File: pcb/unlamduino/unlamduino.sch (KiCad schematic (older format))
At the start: 34 parts, among them IC2 ATMEGA328-P, P3 CONN_01X08, P4 CONN_01X10, P5 CONN_01X06, P6 CONN_01X08, SW1 SW_PUSH, U1 LM2576, Y2 16MHz

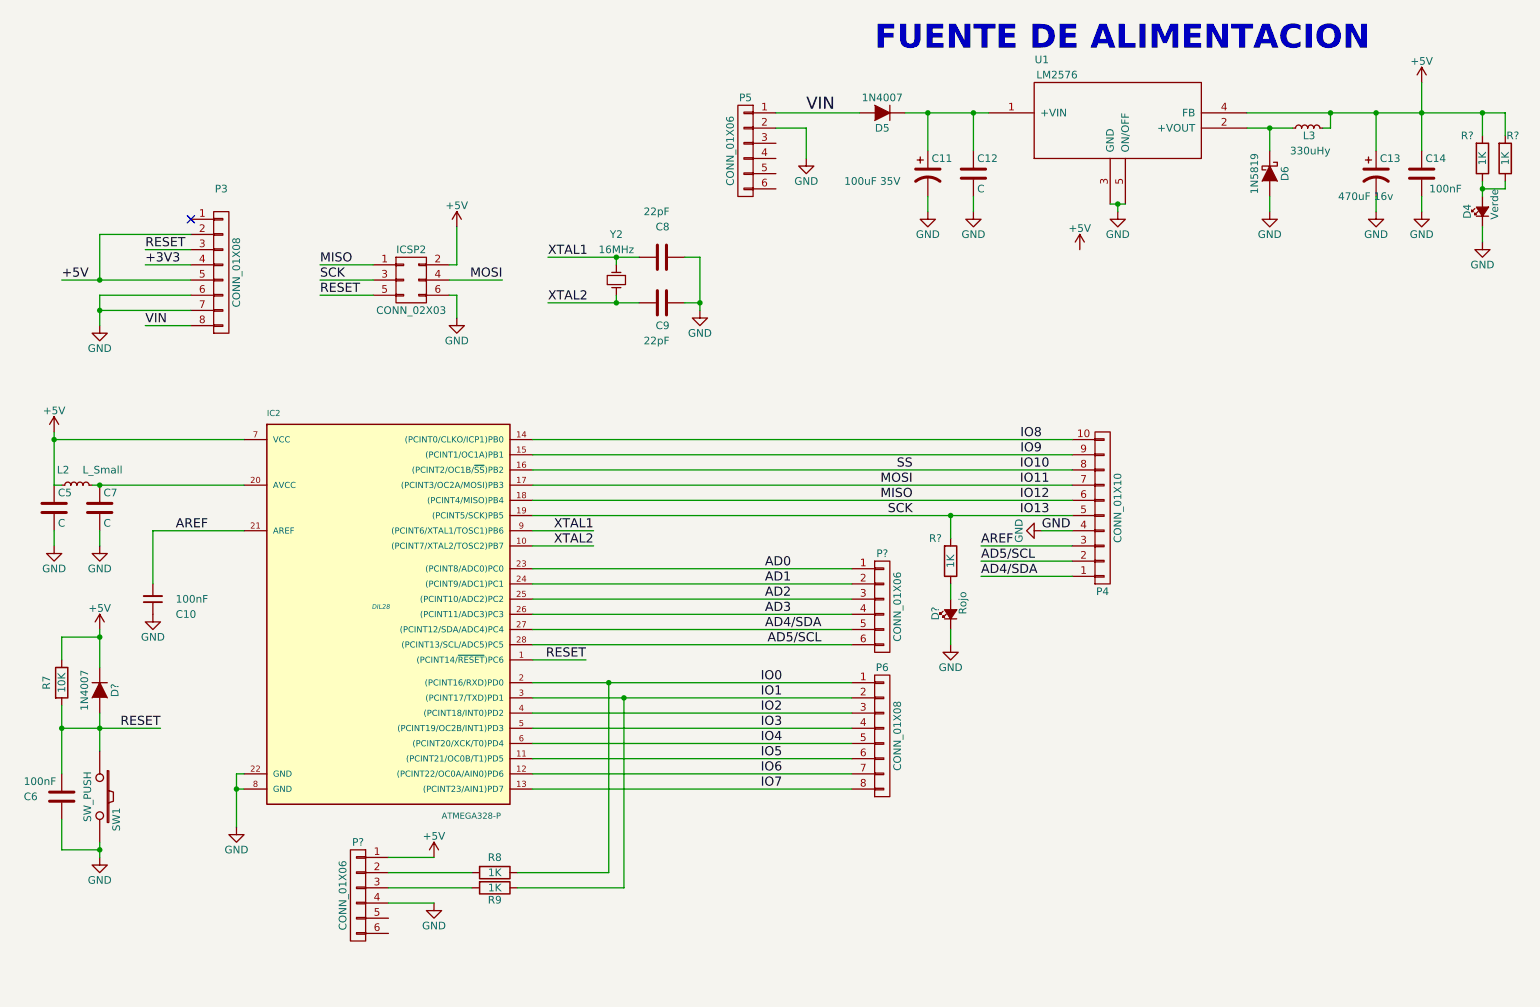
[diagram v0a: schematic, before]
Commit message: Agregado PWR_FLAG y numeracion. Agregado de valores a algunos capacitores.
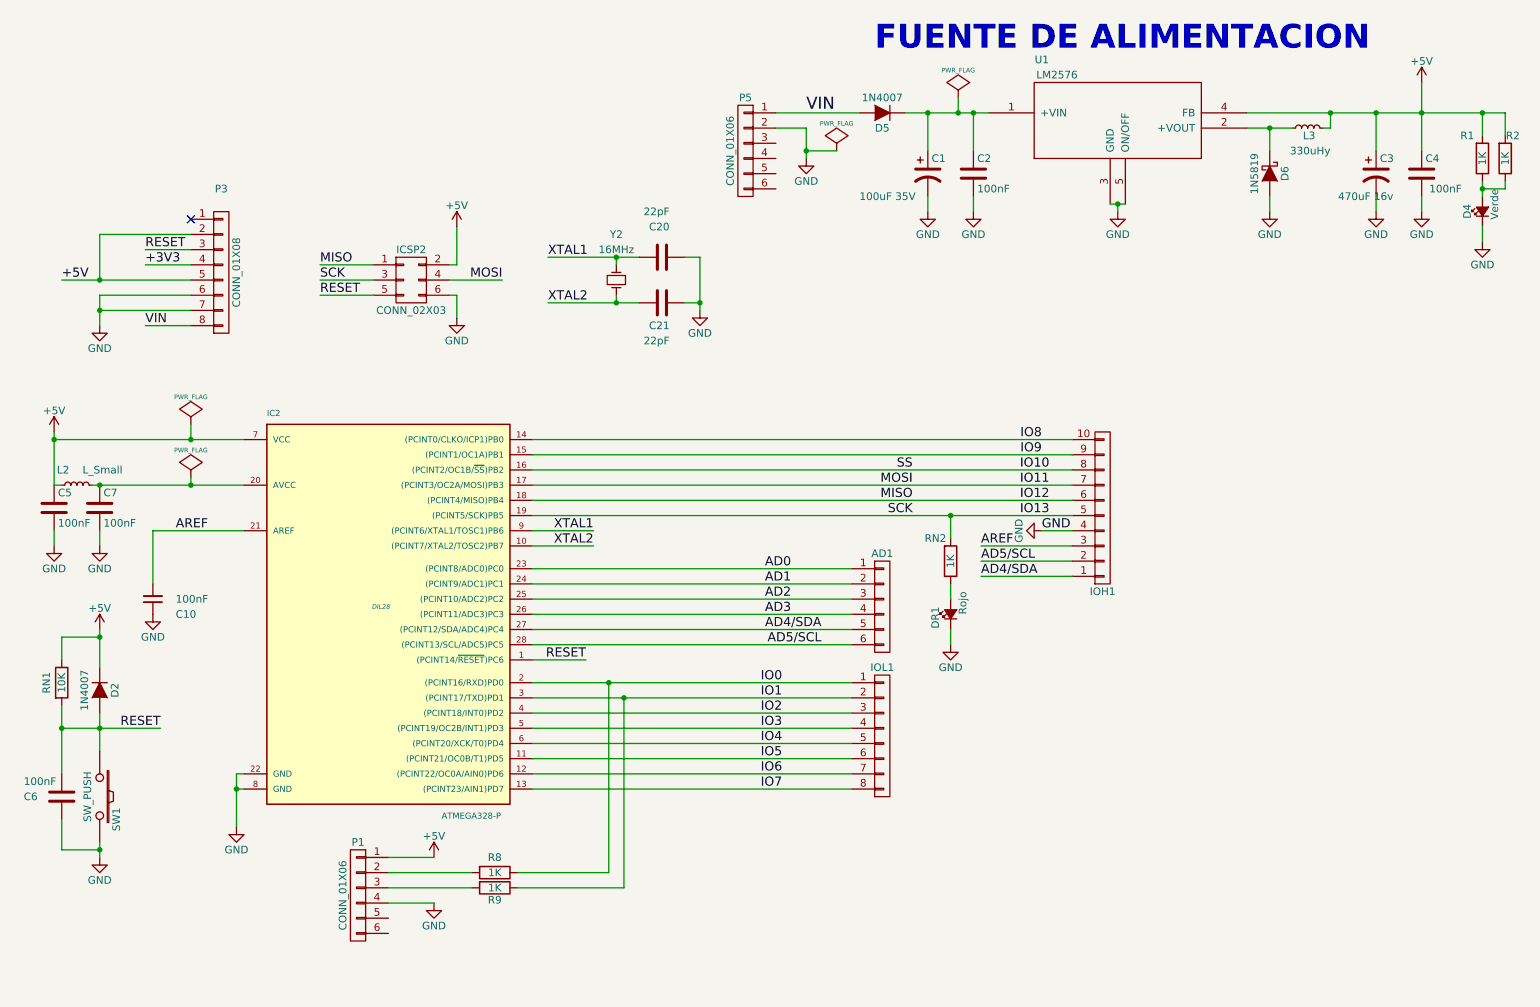
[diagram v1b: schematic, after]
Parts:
- C2: renamed from C12; value C -> 100nF
- C5, C7: value C -> 100nF
- gave numbers to parts that had none: 7
- renumbered C11 to C1, C8 to C20, C9 to C21, C13 to C3, C14 to C4, P4 to IOH1, P6 to IOL1, R7 to RN1

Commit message: Agregado regulador de 3v3 y conectores a utilizar.
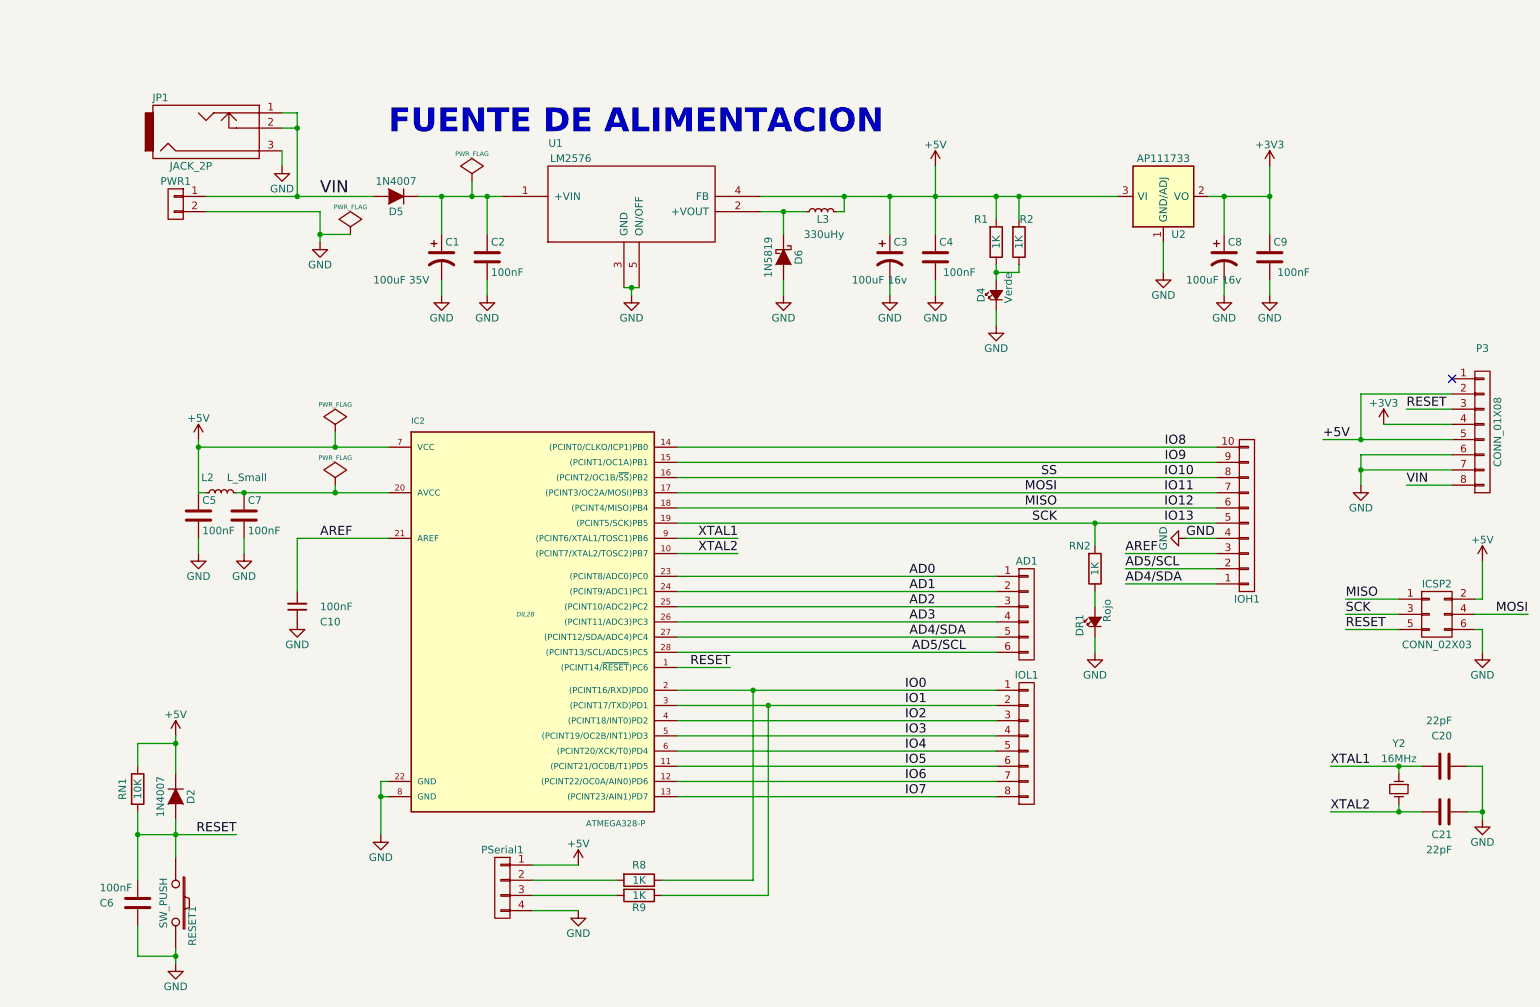
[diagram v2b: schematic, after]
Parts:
- removed P1, P5: CONN_01X06, symbol CONN_01X06
- added C8: 100uF 16v, symbol CP1-RESCUE-UNLAMDIUNO
- added C9: 100nF, symbol C-RESCUE-UNLAMDIUNO
- added JP1: JACK_2P, symbol JACK_2P
- added PSerial1: CONN_01X04, symbol CONN_01X04
- added PWR1: CONN_01X02, symbol CONN_01X02
- added U2: AP111733, TO_SOT_Packages_SMD:SOT-223, symbol AP111733
- C3: value 470uF 16v -> 100uF 16v
- renumbered SW1 to RESET1
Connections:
- net +3V3: now also C8.1, C9.1, U2.2 (VO)
- net +5V: now also PSerial1.1 (P1), U2.3 (VI)
- net GND: now also C8.2, C9.2, JP1.3, PSerial1.4 (P4), PWR1.2 (P2), U2.1 (GND/ADJ)
- net VIN: now also JP1.1, JP1.2, PWR1.1 (P1)
- net at R8.2: now also PSerial1.2 (P2)
- net at R9.2: now also PSerial1.3 (P3)
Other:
- moved on the sheet: AD1, C1, C10, C2, C20, C21, C3, C4, C5, C6, C7, D2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

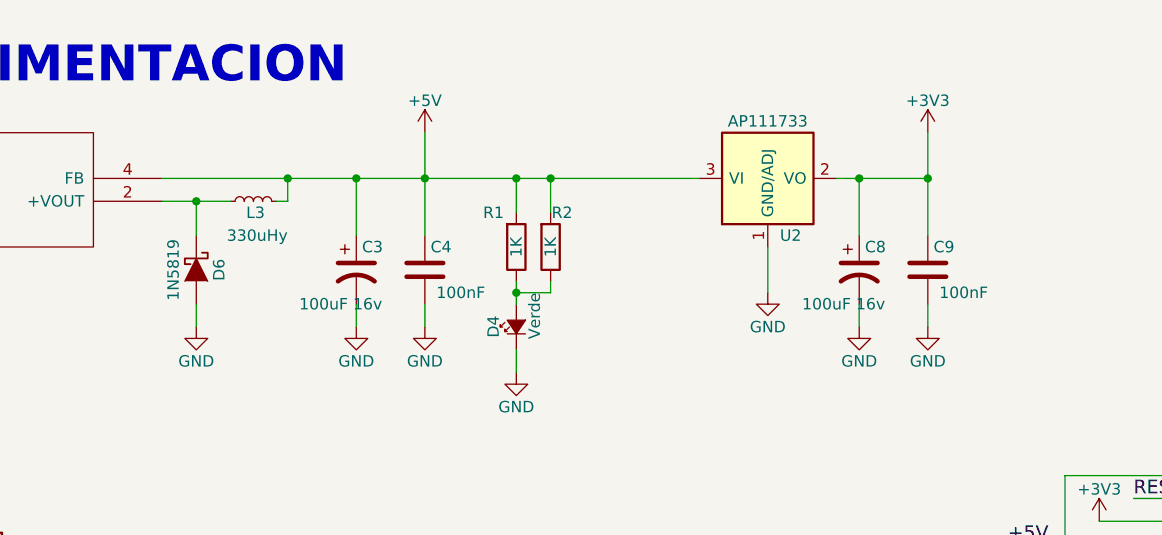
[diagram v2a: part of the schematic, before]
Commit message: Resistor en led de encendido de 470 en vez de 2 de 1K
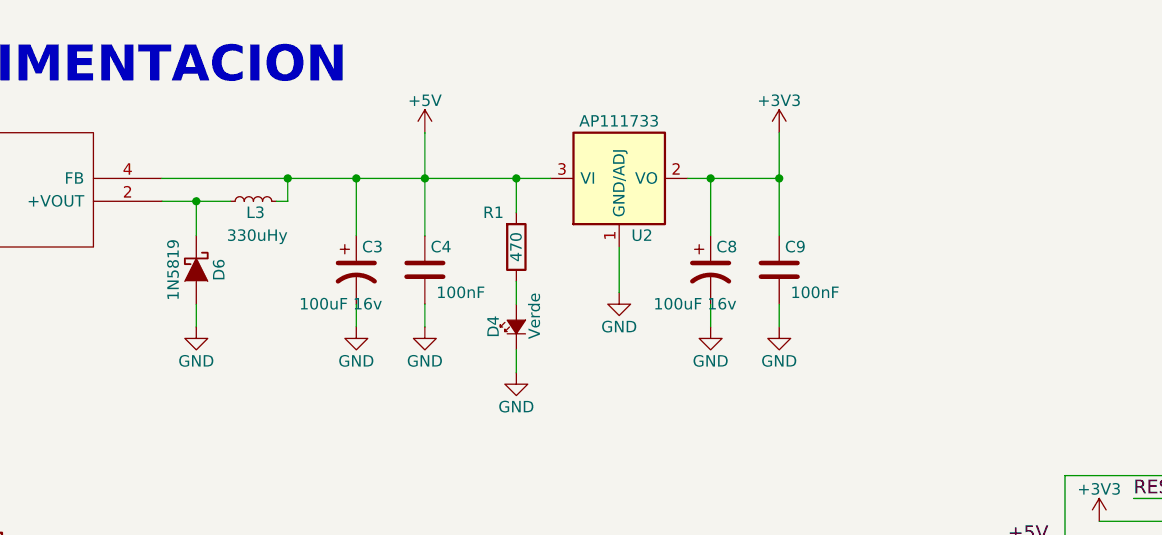
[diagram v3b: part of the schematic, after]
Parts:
- removed R2: 1K, symbol R-RESCUE-UNLAMDIUNO
- R1: value 1K -> 470
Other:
- moved on the sheet: C8, C9, U2
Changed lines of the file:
@@
 	8450 4150 8650 4150
 Wire Wire Line
-	5650 1900 8000 1900
+	5650 1900 7350 1900
 Wire Wire Line
 	7200 1900 7200 2050
-Wire Wire Line
-	7350 1900 7350 2050
 Connection ~ 7200 1900
 Wire Wire Line
 	7200 2350 7200 2450
-Wire Wire Line
-	7350 2350 7350 2400
-Wire Wire Line
-	7350 2400 7200 2400
-Connection ~ 7200 2400
 Wire Wire Line
 	7200 2650 7200 2750
@@
 P 7200 2200
 F 0 "R1" H 7100 2050 50  0000 C CNN
-F 1 "1K" V 7200 2200 50  0000 C CNN
+F 1 "470" V 7200 2200 50  0000 C CNN
 F 2 "" V 7130 2200 50  0000 C CNN
 F 3 "" H 7200 2200 50  0000 C CNN
 	1    7200 2200
-	1    0    0    1
-$EndComp
-$Comp
-L R-RESCUE-UNLAMDIUNO R2
-U 1 1 57F5BEE7
-P 7350 2200
-F 0 "R2" H 7400 2050 50  0000 C CNN
-F 1 "1K" V 7350 2200 50  0000 C CNN
-F 2 "" V 7280 2200 50  0000 C CNN
-F 3 "" H 7350 2200 50  0000 C CNN
-	1    7350 2200
 	1    0    0    1
 $EndComp
@@
 	2500 1450 2600 1450
 Connection ~ 2600 1450
-Connection ~ 7350 1900
 $Comp
 L GND-RESCUE-UNLAMDIUNO #PWR030
 U 1 1 57F5BA04
-P 8300 2400
-F 0 "#PWR030" H 8300 2150 50  0001 C CNN
-F 1 "GND" H 8300 2250 50  0000 C CNN
-F 2 "" H 8300 2400 60  0000 C CNN
-F 3 "" H 8300 2400 60  0000 C CNN
-	1    8300 2400
+P 7650 2400
+F 0 "#PWR030" H 7650 2150 50  0001 C CNN
+F 1 "GND" H 7650 2250 50  0000 C CNN
+F 2 "" H 7650 2400 60  0000 C CNN
+F 3 "" H 7650 2400 60  0000 C CNN
+	1    7650 2400
 	-1   0    0    -1
 $EndComp
 Wire Wire Line
-	8300 2200 8300 2400
-Wire Wire Line
-	8700 1900 8700 2150
-Wire Wire Line
-	9000 1700 9000 2150
-Wire Wire Line
-	9000 2450 9000 2550
+	7650 2200 7650 2400
+Wire Wire Line
+	8050 1900 8050 2150
+Wire Wire Line
+	8350 1700 8350 2150
+Wire Wire Line
+	8350 2450 8350 2550
 $Comp
 L GND-RESCUE-UNLAMDIUNO #PWR031
 U 1 1 57F5C1ED
-P 9000 2550
-F 0 "#PWR031" H 9000 2300 50  0001 C CNN
-F 1 "GND" H 9000 2400 50  0000 C CNN
-F 2 "" H 9000 2550 50  0000 C CNN
-F 3 "" H 9000 2550 50  0000 C CNN
-	1    9000 2550
-	1    0    0    -1
-$EndComp
-Wire Wire Line
-	8700 2450 8700 2550
+P 8350 2550
+F 0 "#PWR031" H 8350 2300 50  0001 C CNN
+F 1 "GND" H 8350 2400 50  0000 C CNN
+F 2 "" H 8350 2550 50  0000 C CNN
+F 3 "" H 8350 2550 50  0000 C CNN
+	1    8350 2550
+	1    0    0    -1
+$EndComp
+Wire Wire Line
+	8050 2450 8050 2550
 $Comp
 L GND-RESCUE-UNLAMDIUNO #PWR032
 U 1 1 57F5C1F4
-P 8700 2550
-F 0 "#PWR032" H 8700 2300 50  0001 C CNN
-F 1 "GND" H 8700 2400 50  0000 C CNN
-F 2 "" H 8700 2550 50  0000 C CNN
-F 3 "" H 8700 2550 50  0000 C CNN
-	1    8700 2550
+P 8050 2550
+F 0 "#PWR032" H 8050 2300 50  0001 C CNN
+F 1 "GND" H 8050 2400 50  0000 C CNN
+F 2 "" H 8050 2550 50  0000 C CNN
+F 3 "" H 8050 2550 50  0000 C CNN
+	1    8050 2550
 	1    0    0    -1
 $EndComp
@@
 L C-RESCUE-UNLAMDIUNO C9
 U 1 1 57F5C1FA
-P 9000 2300
-F 0 "C9" H 9025 2400 50  0000 L CNN
-F 1 "100nF" H 9050 2200 50  0000 L CNN
-F 2 "" H 9038 2150 50  0000 C CNN
-F 3 "" H 9000 2300 50  0000 C CNN
-	1    9000 2300
+P 8350 2300
+F 0 "C9" H 8375 2400 50  0000 L CNN
+F 1 "100nF" H 8400 2200 50  0000 L CNN
+F 2 "" H 8388 2150 50  0000 C CNN
+F 3 "" H 8350 2300 50  0000 C CNN
+	1    8350 2300
 	1    0    0    -1
 $EndComp
@@
 L CP1-RESCUE-UNLAMDIUNO C8
 U 1 1 57F5C200
-P 8700 2300
-F 0 "C8" H 8725 2400 50  0000 L CNN
-F 1 "100uF 16v" H 8450 2150 50  0000 L CNN
-F 2 "" H 8700 2300 50  0000 C CNN
-F 3 "" H 8700 2300 50  0000 C CNN
-	1    8700 2300
-	1    0    0    -1
-$EndComp
-Wire Wire Line
-	8600 1900 9000 1900
-Connection ~ 9000 1900
-Connection ~ 8700 1900
+P 8050 2300
+F 0 "C8" H 8075 2400 50  0000 L CNN
+F 1 "100uF 16v" H 7800 2150 50  0000 L CNN
+F 2 "" H 8050 2300 50  0000 C CNN
+F 3 "" H 8050 2300 50  0000 C CNN
+	1    8050 2300
+	1    0    0    -1
+$EndComp
+Wire Wire Line
+	7950 1900 8350 1900
+Connection ~ 8350 1900
+Connection ~ 8050 1900
 $Comp
 L +3V3 #PWR033
 U 1 1 57F5C683
-P 9000 1700
-F 0 "#PWR033" H 9000 1550 50  0001 C CNN
-F 1 "+3V3" H 9000 1840 50  0000 C CNN
-F 2 "" H 9000 1700 50  0000 C CNN
-F 3 "" H 9000 1700 50  0000 C CNN
-	1    9000 1700
+P 8350 1700
+F 0 "#PWR033" H 8350 1550 50  0001 C CNN
+F 1 "+3V3" H 8350 1840 50  0000 C CNN
+F 2 "" H 8350 1700 50  0000 C CNN
+F 3 "" H 8350 1700 50  0000 C CNN
+	1    8350 1700
 	1    0    0    -1
 $EndComp
@@
 L AP111733 U2
 U 1 1 57F5E03B
-P 8300 1900
-F 0 "U2" H 8400 1650 50  0000 C CNN
-F 1 "AP111733" H 8300 2150 50  0000 C CNN
-F 2 "TO_SOT_Packages_SMD:SOT-223" H 8300 1550 50  0001 C CNN
-F 3 "" H 8400 1650 50  0000 C CNN
-	1    8300 1900
-	1    0    0    -1
-$EndComp
+P 7650 1900
+F 0 "U2" H 7750 1650 50  0000 C CNN
+F 1 "AP111733" H 7650 2150 50  0000 C CNN
+F 2 "TO_SOT_Packages_SMD:SOT-223" H 7650 1550 50  0001 C CNN
+F 3 "" H 7750 1650 50  0000 C CNN
+	1    7650 1900
+	1    0    0    -1
+$EndComp
